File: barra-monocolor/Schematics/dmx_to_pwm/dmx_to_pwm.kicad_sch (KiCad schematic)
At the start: 53 parts, among them J1 RJ45, J2 RJ45, J3 Conn_02x04_Top_Bottom, J4 Conn_01x03_Socket, J5 Conn_01x05_Socket, Q1 TIP41, Q2 TIP41, Q3 TIP41, Q5 TIP41, SW1 SW_DIP_x08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

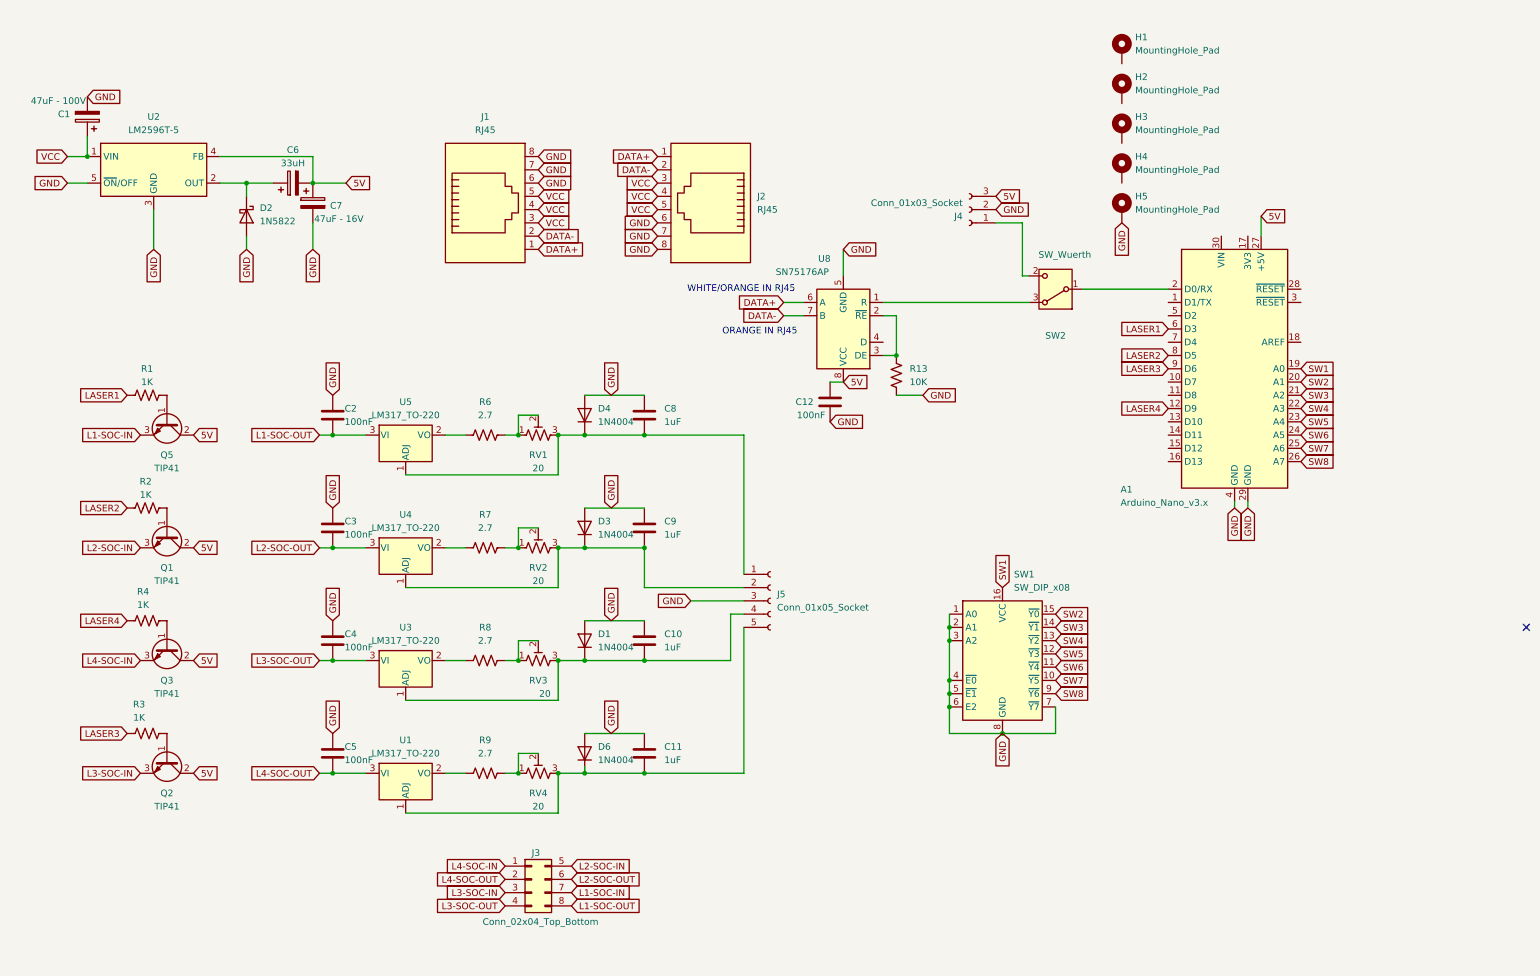
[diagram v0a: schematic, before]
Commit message: updated schematics to 6 lasers
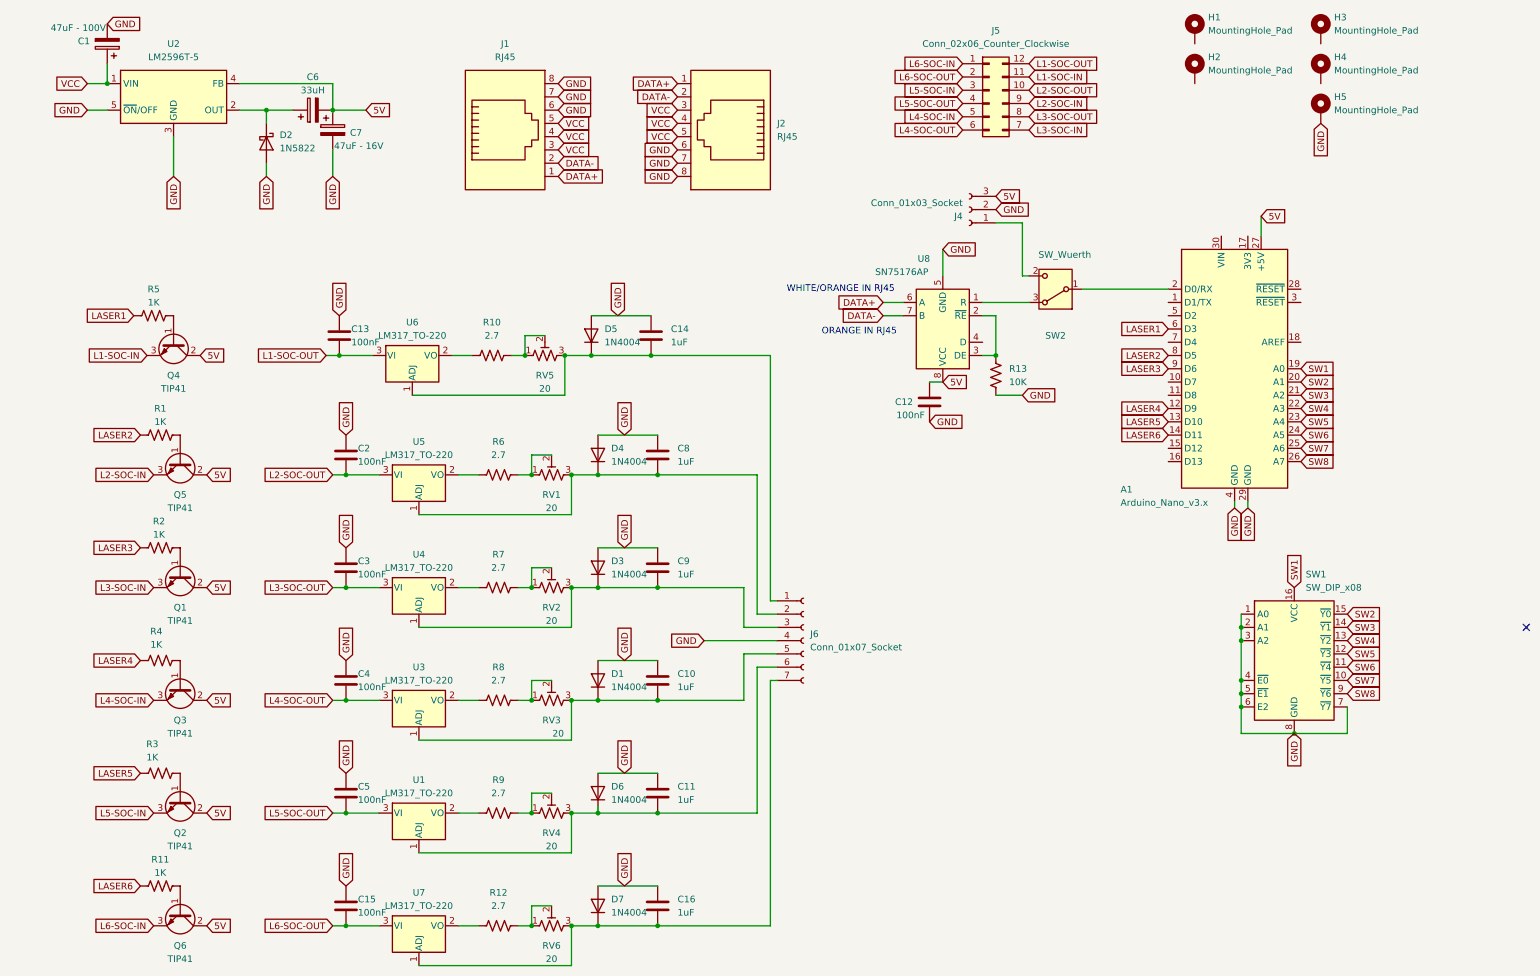
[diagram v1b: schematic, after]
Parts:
- removed J3: Conn_02x04_Top_Bottom, Connector_PinHeader_2.54mm:PinHeader_2x04_P2.54mm_Vertical, symbol Connector_Generic:Conn_02x04_Top_Bottom
- removed J5: Conn_01x05_Socket, Connector_JST:JST_EH_B5B-EH-A_1x05_P2.50mm_Vertical, symbol Connector:Conn_01x05_Socket
- added C13, C15: 100nF, Capacitor_THT:C_Disc_D3.0mm_W2.0mm_P2.50mm, symbol Device:C
- added C14, C16: 1uF, Capacitor_THT:C_Disc_D3.0mm_W2.0mm_P2.50mm, symbol Device:C
- added D5, D7: 1N4004, Diode_THT:D_DO-41_SOD81_P7.62mm_Horizontal, symbol Diode:1N4004
- added J5: Conn_02x06_Counter_Clockwise, Connector_PinHeader_2.54mm:PinHeader_2x06_P2.54mm_Vertical, symbol Connector_Generic:Conn_02x06_Counter_Clockwise
- added J6: Conn_01x07_Socket, Connector_JST:JST_EH_B7B-EH-A_1x07_P2.50mm_Vertical, symbol Connector:Conn_01x07_Socket
- added Q4, Q6: TIP41, Package_TO_SOT_THT:TO-220-3_Vertical, symbol Transistor_BJT:TIP41
- added R10, R12: 2.7, Resistor_THT:R_Axial_DIN0411_L9.9mm_D3.6mm_P12.70mm_Horizontal, symbol Device:R_US
- added R11, R5: 1K, Resistor_THT:R_Axial_DIN0207_L6.3mm_D2.5mm_P7.62mm_Horizontal, symbol Device:R_US
- added RV5, RV6: 20, Potentiometer_THT:Potentiometer_Bourns_3296Z_Horizontal, symbol Device:R_Potentiometer_Trim_US
- added U6, U7: LM317_TO-220, Package_TO_SOT_THT:TO-220-3_Vertical, symbol Regulator_Linear:LM317_TO-220
- R1, R2, R3, R4: footprint Resistor_THT:R_Axial_DIN0414_L11.9mm_D4.5mm_P7.62mm_Vertical -> Resistor_THT:R_Axial_DIN0207_L6.3mm_D2.5mm_P7.62mm_Horizontal
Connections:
- net 5V: now also Q4.2 (C), Q6.2 (C)
- net GND: now also C13.1, C14.1, C15.1, C16.1, D5.2 (A), D7.2 (A), J6.4 (Pin_4)
- net L1-SOC-IN: now also J5.11 (Pin_11), Q4.3 (E); no longer Q5.3 (E)
- net L1-SOC-OUT: now also C13.2, J5.12 (Pin_12), U6.3 (VI); no longer C2.2, U5.3 (VI)
- net L2-SOC-IN: now also Q5.3 (E), J5.9 (Pin_9); no longer Q1.3 (E)
- net L2-SOC-OUT: now also C2.2, U5.3 (VI), J5.10 (Pin_10); no longer C3.2, U4.3 (VI)
- net L3-SOC-IN: now also Q1.3 (E), J5.7 (Pin_7); no longer Q2.3 (E)
- net L3-SOC-OUT: now also C3.2, U4.3 (VI), J5.8 (Pin_8); no longer C4.2, U3.3 (VI)
- net L4-SOC-IN: now also J5.5 (Pin_5)
- net L4-SOC-OUT: now also C4.2, U3.3 (VI), J5.6 (Pin_6); no longer C5.2, U1.3 (VI)
- net LASER1: now also R5.2; no longer R1.2
- net LASER2: now also R1.2; no longer R2.2
- net LASER3: now also R2.2; no longer R3.2
- net at C10.2, D1.1 (K), RV3.3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: now also J6.5 (Pin_5)
- net at C8.2, D4.1 (K), RV1.3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: now also J6.2 (Pin_2)
- net at C9.2, D3.1 (K), RV2.3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: now also J6.3 (Pin_3)
- net at C11.2, D6.1 (K), RV4.3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: now also J6.6 (Pin_6)
- net LASER5: now reaches A1.13 (D10)
- net LASER5: now also R3.2
- net LASER6: now reaches A1.14 (D11)
- net LASER6: now also R11.2
- new net: C16.2, D7.1 (K), J6.7 (Pin_7), RV6.3, U7.1 (ADJ)
- new net: Q4.1 (B), R5.1
- new net: R12.1, RV6.1, RV6.2
- new net: R10.1, RV5.1, RV5.2
- new net: C14.2, D5.1 (K), J6.1 (Pin_1), RV5.3, U6.1 (ADJ)
- new net: Q6.1 (B), R11.1
- new net: R12.2, U7.2 (VO)
- new net: R10.2, U6.2 (VO)
- new net L5-SOC-IN: J5.3 (Pin_3), Q2.3 (E)
- new net L5-SOC-OUT: C5.2, J5.4 (Pin_4), U1.3 (VI)
- new net L6-SOC-IN: J5.1 (Pin_1), Q6.3 (E)
- new net L6-SOC-OUT: C15.2, J5.2 (Pin_2), U7.3 (VI)
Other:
- moved on the sheet: C1, C10, C11, C12, C2, C3, C4, C5, C6, C7, C8, C9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

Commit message: updated pcb for 6 lasers
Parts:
- removed H5: MountingHole_Pad, MountingHole:MountingHole_3.2mm_M3_Pad, symbol Mechanical:MountingHole_Pad
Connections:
- net GND: now also H4.1
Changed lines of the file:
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@@
 	(global_label "GND"
 		(shape input)
-		(at 260.35 35.56 270)
+		(at 260.35 27.94 270)
 		(fields_autoplaced yes)
 		(effects
@@
 		)
 		(property "Intersheetrefs" "${INTERSHEET_REFS}"
-			(at 260.35 42.4157 90)
+			(at 260.35 34.7957 90)
 			(effects
 				(font
@@
 					(unit 1)
 				)
-			)
-		)
-	)
-	(symbol
-		(lib_id "Mechanical:MountingHole_Pad")
-		(at 260.35 33.02 0)
-		(unit 1)
-		(exclude_from_sim yes)
-		(in_bom no)
-		(on_board yes)
-		(dnp no)
-		(fields_autoplaced yes)
-		(property "Reference" "H5"
-			(at 262.89 30.4799 0)
-			(effects
-				(font
-					(size 1.27 1.27)
-				)
-				(justify left)
-			)
-		)
-		(property "Value" "MountingHole_Pad"
-			(at 262.89 33.0199 0)
-			(effects
-				(font
-					(size 1.27 1.27)
-				)
-				(justify left)
-			)
-		)
-		(property "Footprint" "MountingHole:MountingHole_3.2mm_M3_Pad"
-			(at 260.35 33.02 0)
-			(effects
-				(font
-					(size 1.27 1.27)
-				)
-				(hide yes)
-			)
-		)
-		(property "Datasheet" "~"
-			(at 260.35 33.02 0)
-			(effects
-				(font
-					(size 1.27 1.27)
-				)
-				(hide yes)
-			)
-		)
-		(property "Description" "Mounting Hole with connection"
-			(at 260.35 33.02 0)
-			(effects
-				(font
-					(size 1.27 1.27)
-				)
-				(hide yes)
-			)
-		)
-		(pin "1"
-		)
-		(instances
-			(project ""
-				(path "/fe39f169-33b8-46fd-886b-c754b4eb741b"
-					(reference "H5")
-					(unit 1)
-				)
